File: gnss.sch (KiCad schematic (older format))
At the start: 9 parts, among them U2301 MAX-M8Q

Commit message: Assign jumper header footprints and component properties, selected based on required current rating and minimized area occupied, assigned 1.5mm diameter test points
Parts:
- AE2301: value ACM4‐5036‐A1‐CC‐S -> ACM4-5036-A1-CC-S; Distrib PN ACM4‐5036‐A1‐CC‐S -> ACM4-5036-A1-CC-S; MFG Part Num ACM4‐5036‐A1‐CC‐S -> ACM4-5036-A1-CC-S
- U2301: value MAX-M8Q -> MAX-8Q; symbol MAX-M8 -> MAX-8; Distrib Link https://www.u-blox.com/en/product/max-m8-series -> https://www.u-blox.com/en/product/max-8-series; Distrib PN MAX-M8Q -> MAX-8Q; MFG Part Num MAX-M8Q -> MAX-8Q
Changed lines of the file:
@@
 $EndDescr
 $Comp
-L MAX-M8 U2301
+L MAX-8 U2301
 U 1 1 5B0DFDBF
 P 5700 3700
 F 0 "U2301" H 5400 4550 60  0000 C CNN
-F 1 "MAX-M8Q" H 5950 4550 60  0000 C CNN
+F 1 "MAX-8Q" H 5950 4550 60  0000 C CNN
 F 2 "dvk-mx8m-bsb:MAX-M8" H 6550 4050 60  0001 C CNN
-F 3 "https://www.u-blox.com/sites/default/files/MAX-M8-FW3_DataSheet_%28UBX-15031506%29.pdf" H 6550 4050 60  0001 C CNN
+F 3 "https://www.u-blox.com/sites/default/files/MAX-8_DataSheet_%28UBX-16000093%29.pdf" H 6550 4050 60  0001 C CNN
 F 4 "U-Blox" H 5700 3700 60  0001 C CNN "MFG Name"
-F 5 "MAX-M8Q" H 5700 3700 60  0001 C CNN "MFG Part Num"
-F 6 "MAX-M8Q" H 5700 3700 60  0001 C CNN "Distrib PN"
-F 7 "https://www.u-blox.com/en/product/max-m8-series" H 5700 3700 60  0001 C CNN "Distrib Link"
+F 5 "MAX-8Q" H 5700 3700 60  0001 C CNN "MFG Part Num"
+F 6 "MAX-8Q" H 5700 3700 60  0001 C CNN "Distrib PN"
+F 7 "https://www.u-blox.com/en/product/max-8-series" H 5700 3700 60  0001 C CNN "Distrib Link"
 F 8 "-" H 5700 3700 60  0001 C CNN "Tolerance"
 F 9 "https://www.digikey.com/product-detail/en/u-blox-america-inc/MAX-M8Q-0/672-1003-1-ND/6150666" H 5700 3700 60  0001 C CNN "Others"
@@
 P 7550 2750
 F 0 "AE2301" H 7900 2900 50  0000 R CNN
-F 1 "ACM4‐5036‐A1‐CC‐S" H 8350 2800 50  0000 R CNN
+F 1 "ACM4-5036-A1-CC-S" H 8500 2800 50  0000 R CNN
 F 2 "" H 7550 2850 50  0001 C CNN
 F 3 "https://www.endrich.com/fm/2/Application%20Note%20no.542665.pdf" H 7550 2850 50  0001 C CNN
 F 4 "INPAQ" H 7550 2750 60  0001 C CNN "MFG Name"
-F 5 "ACM4‐5036‐A1‐CC‐S" H 7550 2750 60  0001 C CNN "MFG Part Num"
-F 6 "ACM4‐5036‐A1‐CC‐S" H 7550 2750 60  0001 C CNN "Distrib PN"
+F 5 "ACM4-5036-A1-CC-S" H 7550 2750 60  0001 C CNN "MFG Part Num"
+F 6 "ACM4-5036-A1-CC-S" H 7550 2750 60  0001 C CNN "Distrib PN"
 F 7 "https://www.endrich.com/antennen_nfc_wpc/acm4_5036_a1_cc_s" H 7550 2750 60  0001 C CNN "Distrib Link"
 F 8 "-" H 7550 2750 60  0001 C CNN "Tolerance"

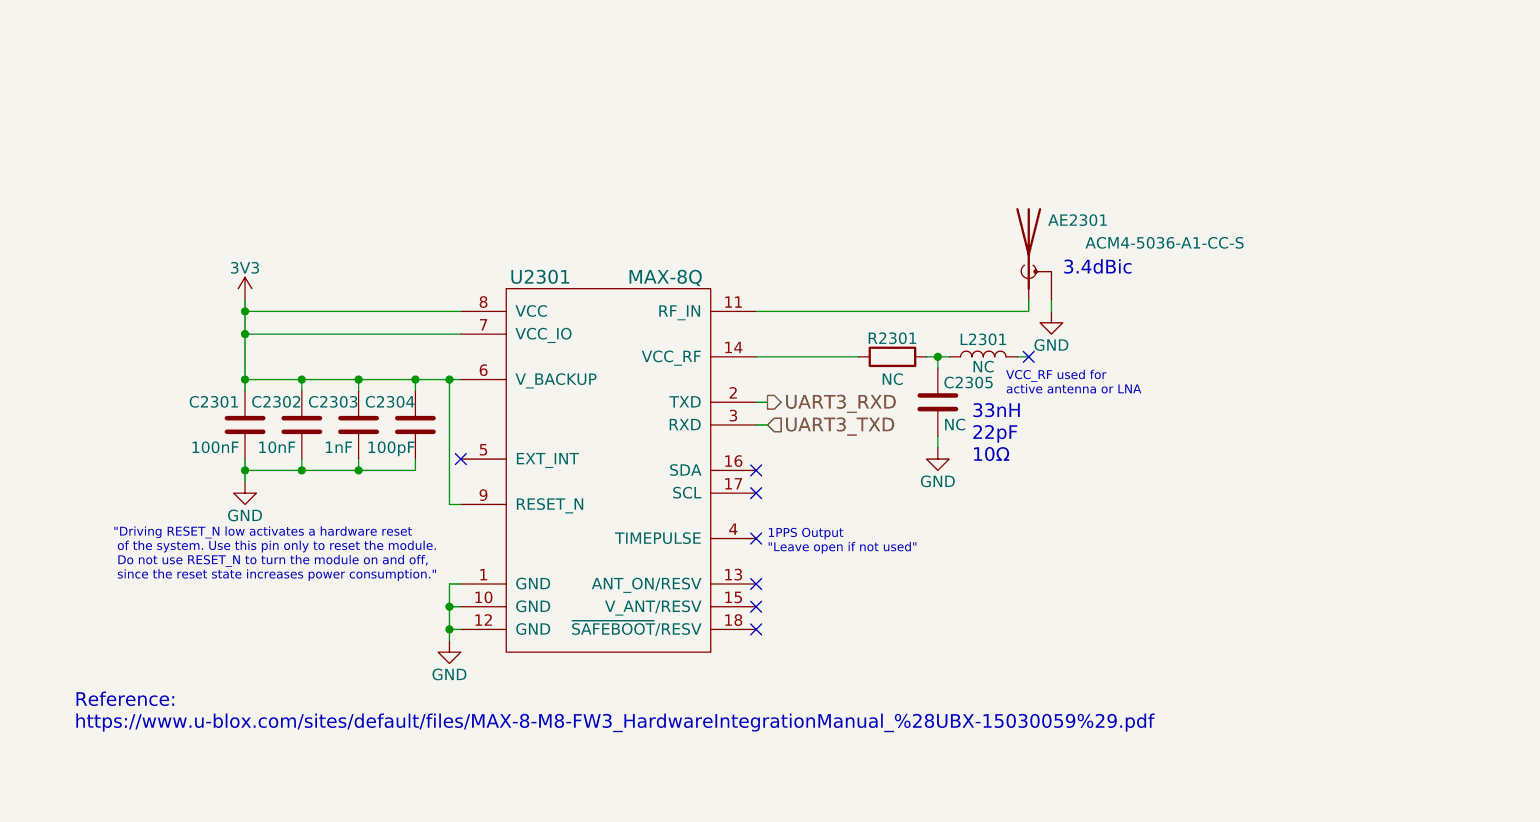
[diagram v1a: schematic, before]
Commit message: Add GNSS antenna footprint including correct 50Ohm feed line dimensions and keepout area, add u-blox MAX-8 3D model, rename all instances of MAX-M8* to MAX-8* due to part selection, antenna feed line calculatos included (coplanar waveguide)
Need to add placeholder footprints for the other four antennae which will be represented as simple rectangular areas where the antennae will occupy. After that, all that is left is to assign the various remaining IC footprints and finally import all footprints into PCBNew & begin layout!
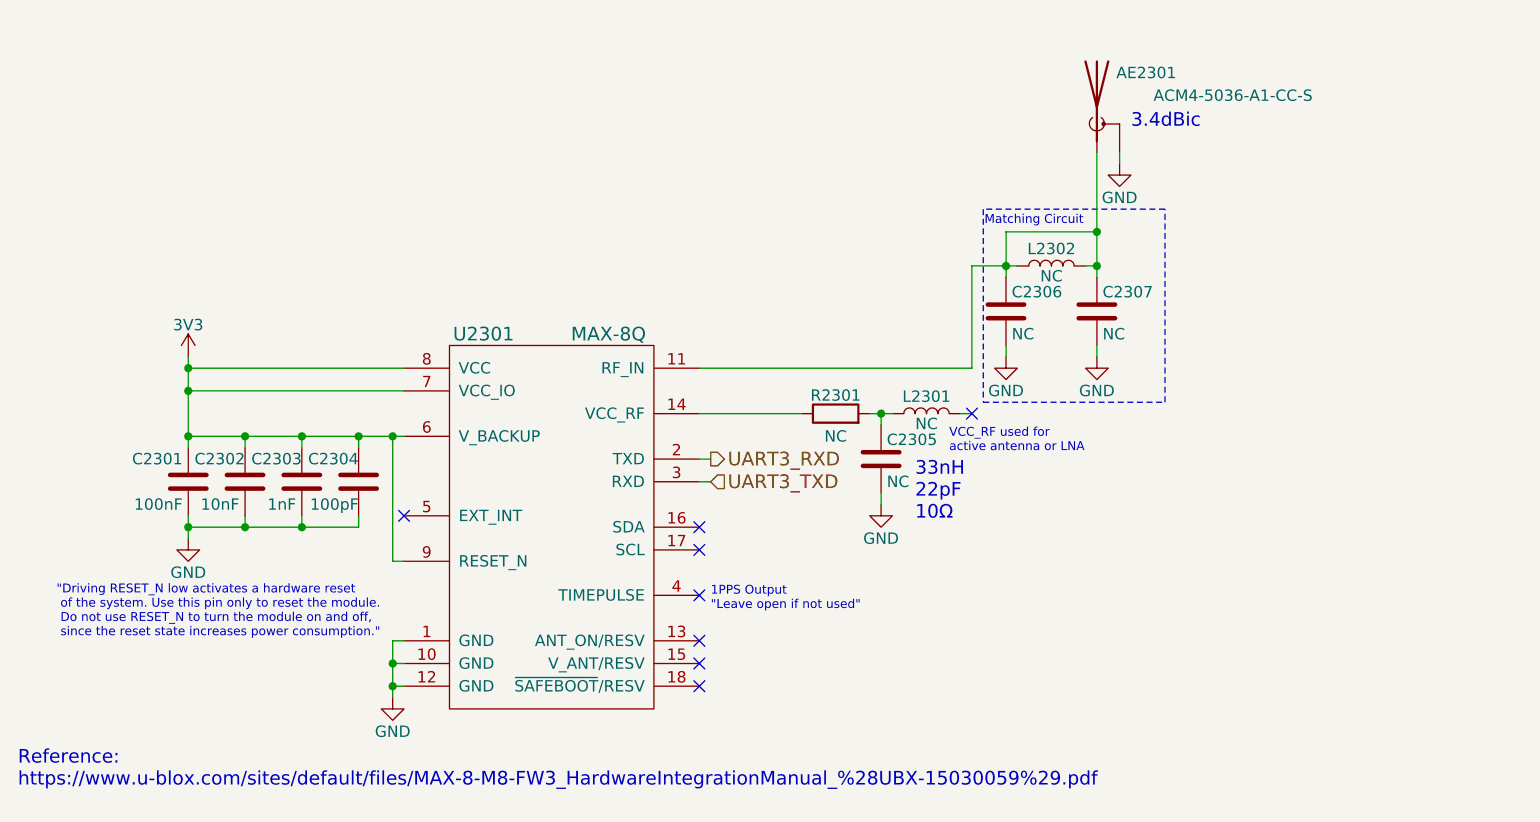
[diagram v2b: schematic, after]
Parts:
- added C2306, C2307: NC, Capacitors_SMD:C_0603, symbol C
- added L2302: NC, Inductors_SMD:L_0603, symbol L
- AE2301: footprint (none) -> dvk-mx8m-bsb:ACM4-5036-A1-CC-S
- U2301: footprint dvk-mx8m-bsb:MAX-M8 -> dvk-mx8m-bsb:MAX-8
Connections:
- net GND: now also C2306.2, C2307.2
- net at AE2301.1 (A), U2301.11 (RF_IN): now also C2306.1, C2307.1, L2302.1, L2302.2
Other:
- note added: "Matching Circuit"
- moved on the sheet: AE2301, C2301, C2302, C2303, C2304, C2305, L2301, R2301, U2301

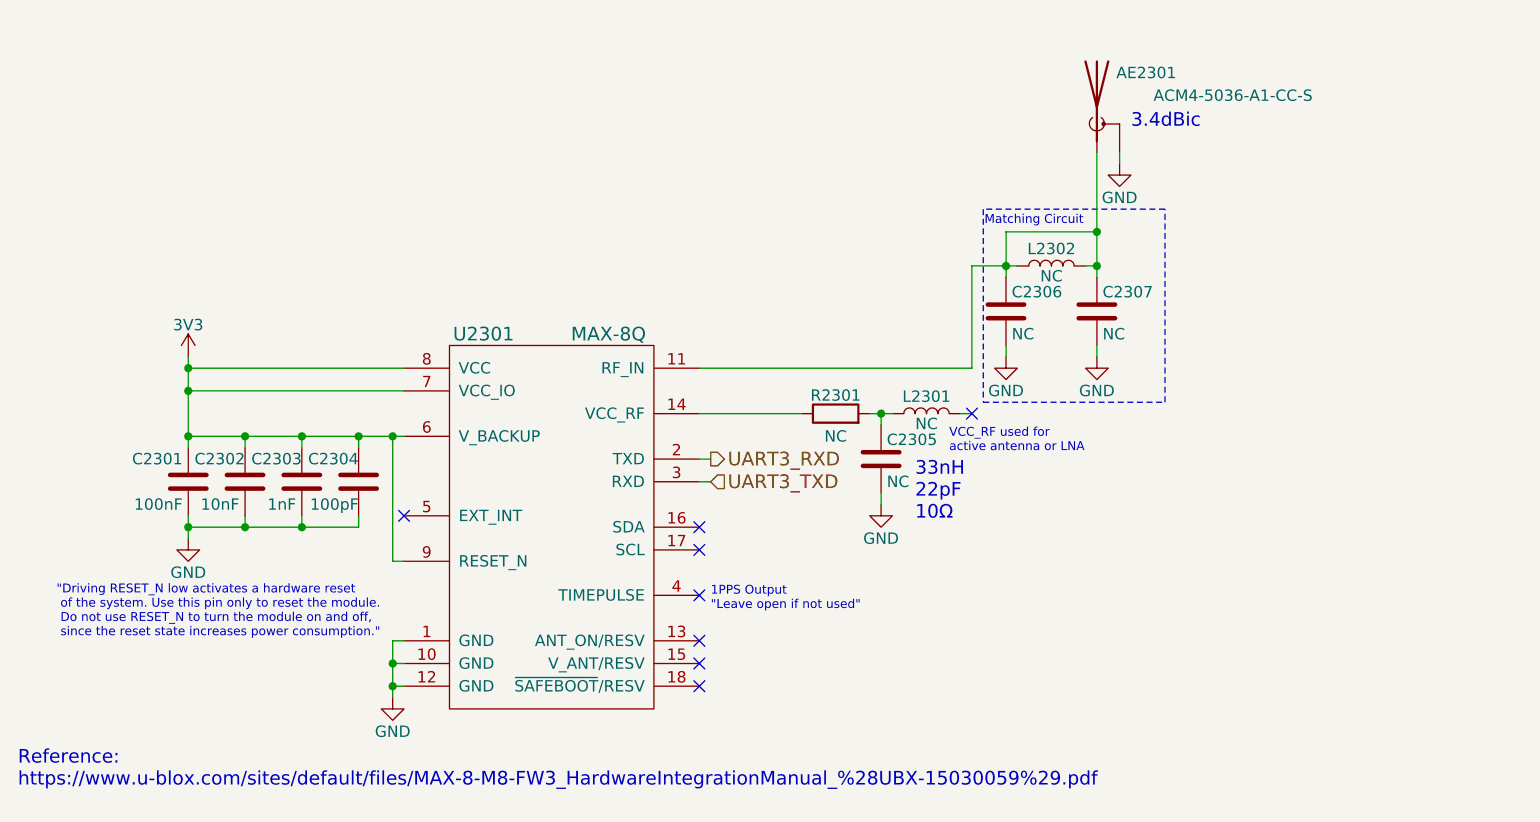
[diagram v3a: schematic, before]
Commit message: Move more symbols, sheets, and pins around on the front sheet to make it even clearer, bring back the old hierarchical structure (again), bring back each sheet's title, add large text "titles" to each sheet reflecting what they are for
Still need to double check everything on the first page.
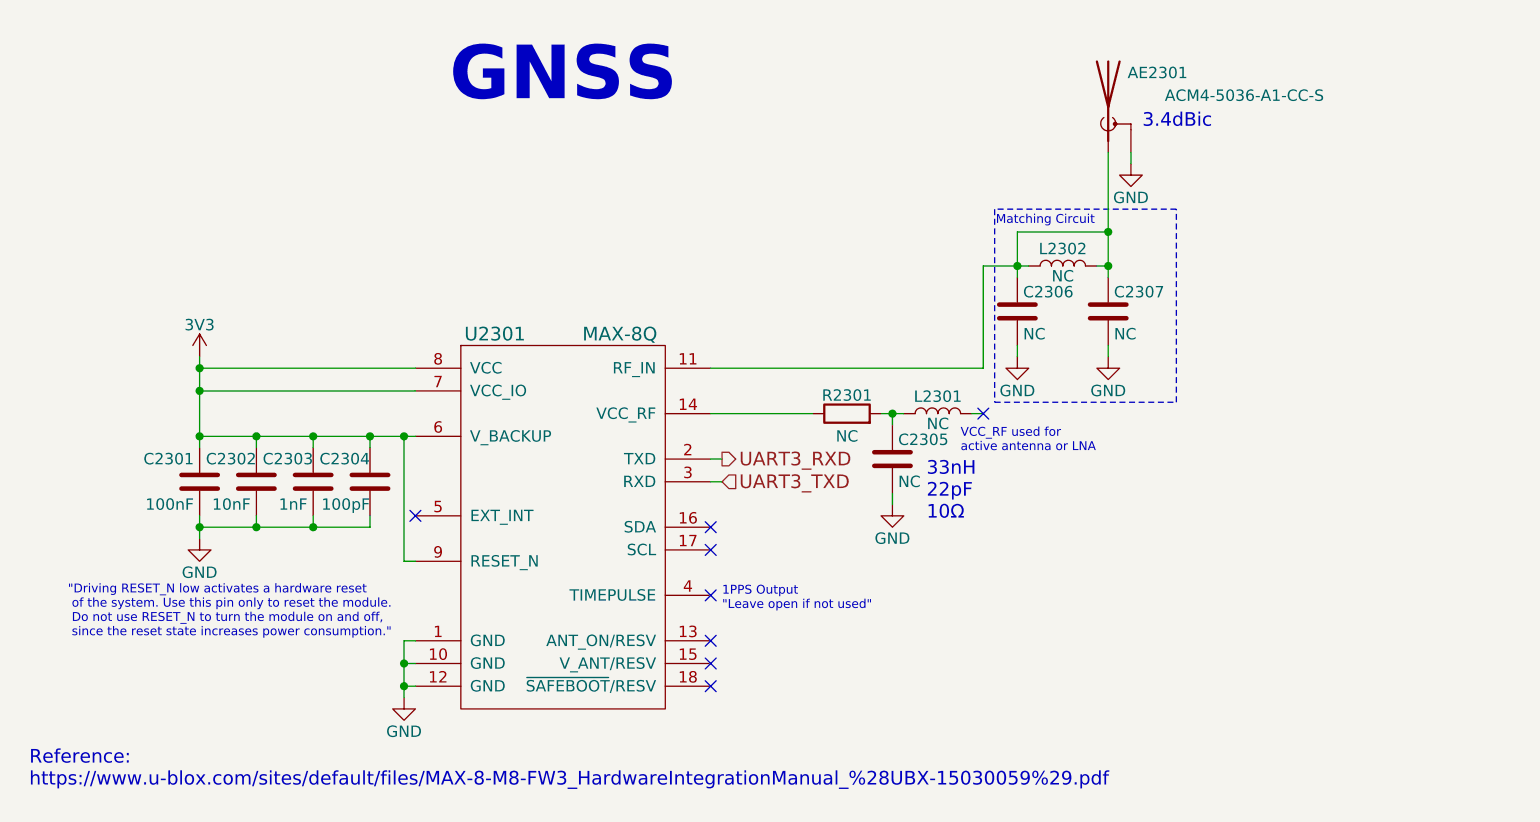
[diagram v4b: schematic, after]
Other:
- note added: "GNSS"
- moved on the sheet: AE2301, C2301, C2302, C2303, C2304, C2305, C2306, C2307, L2301, L2302, R2301, U2301

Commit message: Rename MAX-8 back to MAX-M8 (all references now MAX-M8)
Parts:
- U2301: value MAX-8Q -> MAX-M8Q; footprint dvk-mx8m-bsb:MAX-8 -> dvk-mx8m-bsb:MAX-M8; symbol MAX-8 -> MAX-M8; Distrib Link https://www.u-blox.com/en/product/max-8-series -> https://www.u-blox.com/en/product/max-m8-series; Distrib PN MAX-8Q -> MAX-M8Q; MFG Part Num MAX-8Q -> MAX-M8Q
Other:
- note added: "References:\nhttps://www.u-blox.com/sites/default/files/MAX-M8_HardwareIntegrationManual_%28UBX-13004876%29.pdf\nhttps://www.u-blox.com/sites/default/files/MAX-8-M8-FW3_HardwareIntegrationManual_%28UBX-15030059%29.pdf"
- note removed: "Reference:\nhttps://www.u-blox.com/sites/default/files/MAX-8-M8-FW3_HardwareIntegrationManual_%28UBX-15030059%29.pdf"
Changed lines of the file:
@@
 $EndDescr
-$Comp
-L MAX-8 U2301
-U 1 1 5B0DFDBF
-P 5500 3950
-F 0 "U2301" H 5200 4800 60  0000 C CNN
-F 1 "MAX-8Q" H 5750 4800 60  0000 C CNN
-F 2 "dvk-mx8m-bsb:MAX-8" H 6350 4300 60  0001 C CNN
-F 3 "https://www.u-blox.com/sites/default/files/MAX-8_DataSheet_%28UBX-16000093%29.pdf" H 6350 4300 60  0001 C CNN
-F 4 "U-Blox" H 5500 3950 60  0001 C CNN "MFG Name"
-F 5 "MAX-8Q" H 5500 3950 60  0001 C CNN "MFG Part Num"
-F 6 "MAX-8Q" H 5500 3950 60  0001 C CNN "Distrib PN"
-F 7 "https://www.u-blox.com/en/product/max-8-series" H 5500 3950 60  0001 C CNN "Distrib Link"
-F 8 "-" H 5500 3950 60  0001 C CNN "Tolerance"
-F 9 "https://www.digikey.com/product-detail/en/u-blox-america-inc/MAX-M8Q-0/672-1003-1-ND/6150666" H 5500 3950 60  0001 C CNN "Others"
-	1    5500 3950
-	1    0    0    -1
-$EndComp
 $Comp
 L GND #PWR0369
@@
 	4800 4650 4850 4650
 Connection ~ 4800 4650
-Text Notes 3150 5100 0    60   ~ 0
-Reference:\nhttps://www.u-blox.com/sites/default/files/MAX-8-M8-FW3_HardwareIntegrationManual_%28UBX-15030059%29.pdf
+Text Notes 3150 5150 0    60   ~ 0
+References:\nhttps://www.u-blox.com/sites/default/files/MAX-M8_HardwareIntegrationManual_%28UBX-13004876%29.pdf\nhttps://www.u-blox.com/sites/default/files/MAX-8-M8-FW3_HardwareIntegrationManual_%28UBX-15030059%29.pdf
 Text Notes 8050 2200 0    60   ~ 0
 3.4dBic
@@
 Text Notes 5000 2100 0    236  ~ 47
 GNSS
+$Comp
+L MAX-M8 U2301
+U 1 1 5B0DFDBF
+P 5500 3950
+F 0 "U2301" H 5200 4800 60  0000 C CNN
+F 1 "MAX-M8Q" H 5750 4800 60  0000 C CNN
+F 2 "dvk-mx8m-bsb:MAX-M8" H 6350 4300 60  0001 C CNN
+F 3 "https://www.u-blox.com/sites/default/files/MAX-M8-FW3_DataSheet_%28UBX-15031506%29.pdf" H 6350 4300 60  0001 C CNN
+F 4 "U-Blox" H 5500 3950 60  0001 C CNN "MFG Name"
+F 5 "MAX-M8Q" H 5500 3950 60  0001 C CNN "MFG Part Num"
+F 6 "MAX-M8Q" H 5500 3950 60  0001 C CNN "Distrib PN"
+F 7 "https://www.u-blox.com/en/product/max-m8-series" H 5500 3950 60  0001 C CNN "Distrib Link"
+F 8 "-" H 5500 3950 60  0001 C CNN "Tolerance"
+F 9 "https://www.digikey.com/product-detail/en/u-blox-america-inc/MAX-M8Q-0/672-1003-1-ND/6150666" H 5500 3950 60  0001 C CNN "Others"
+	1    5500 3950
+	1    0    0    -1
+$EndComp
 $EndSCHEMATC
